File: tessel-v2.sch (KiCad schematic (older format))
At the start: 5 parts

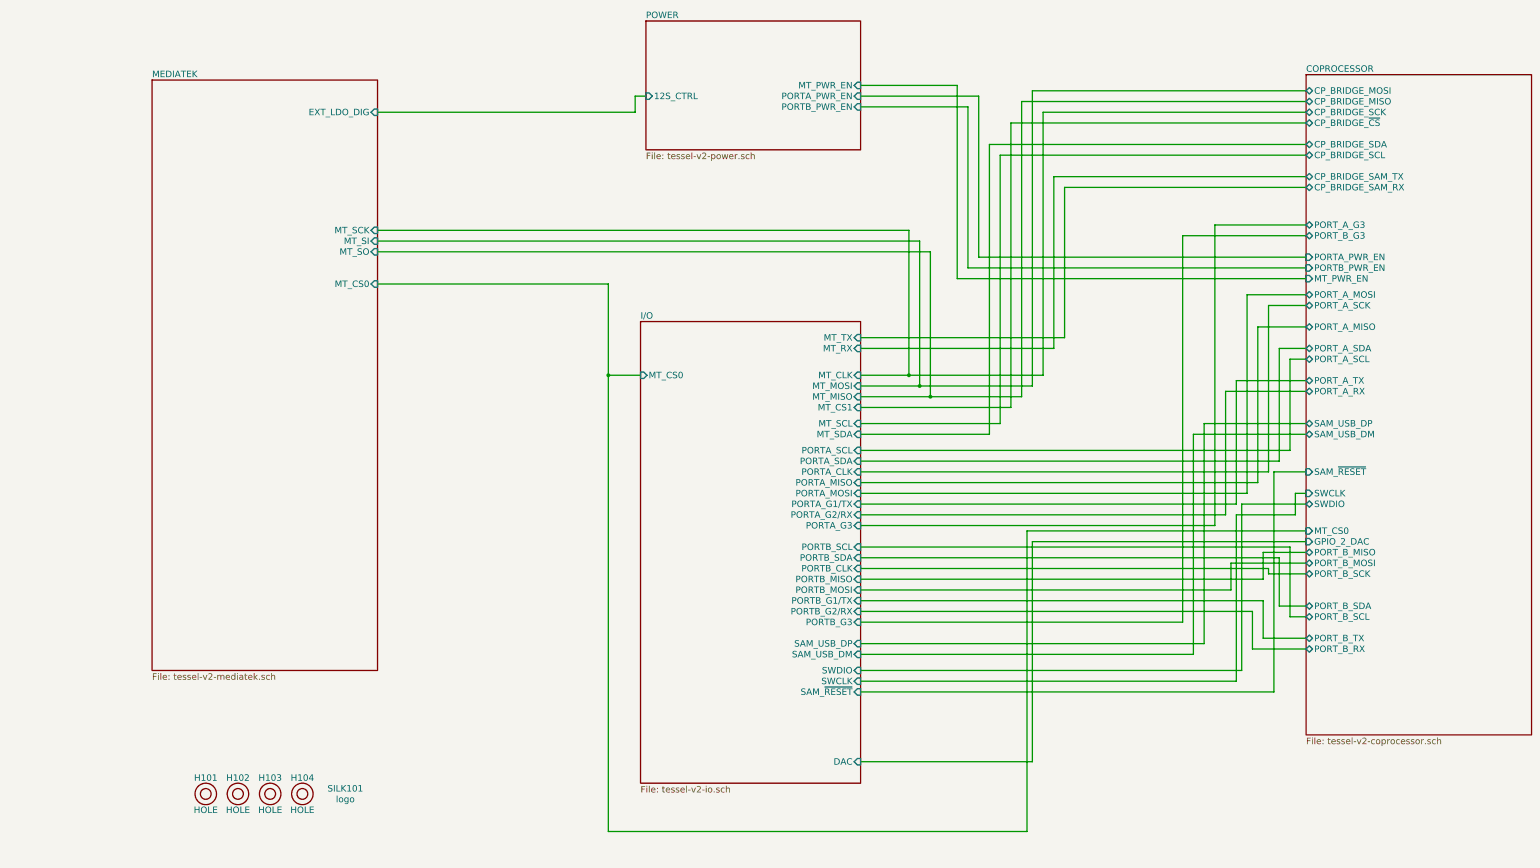
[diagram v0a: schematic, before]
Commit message: most schematic changes done, major refactoring underway
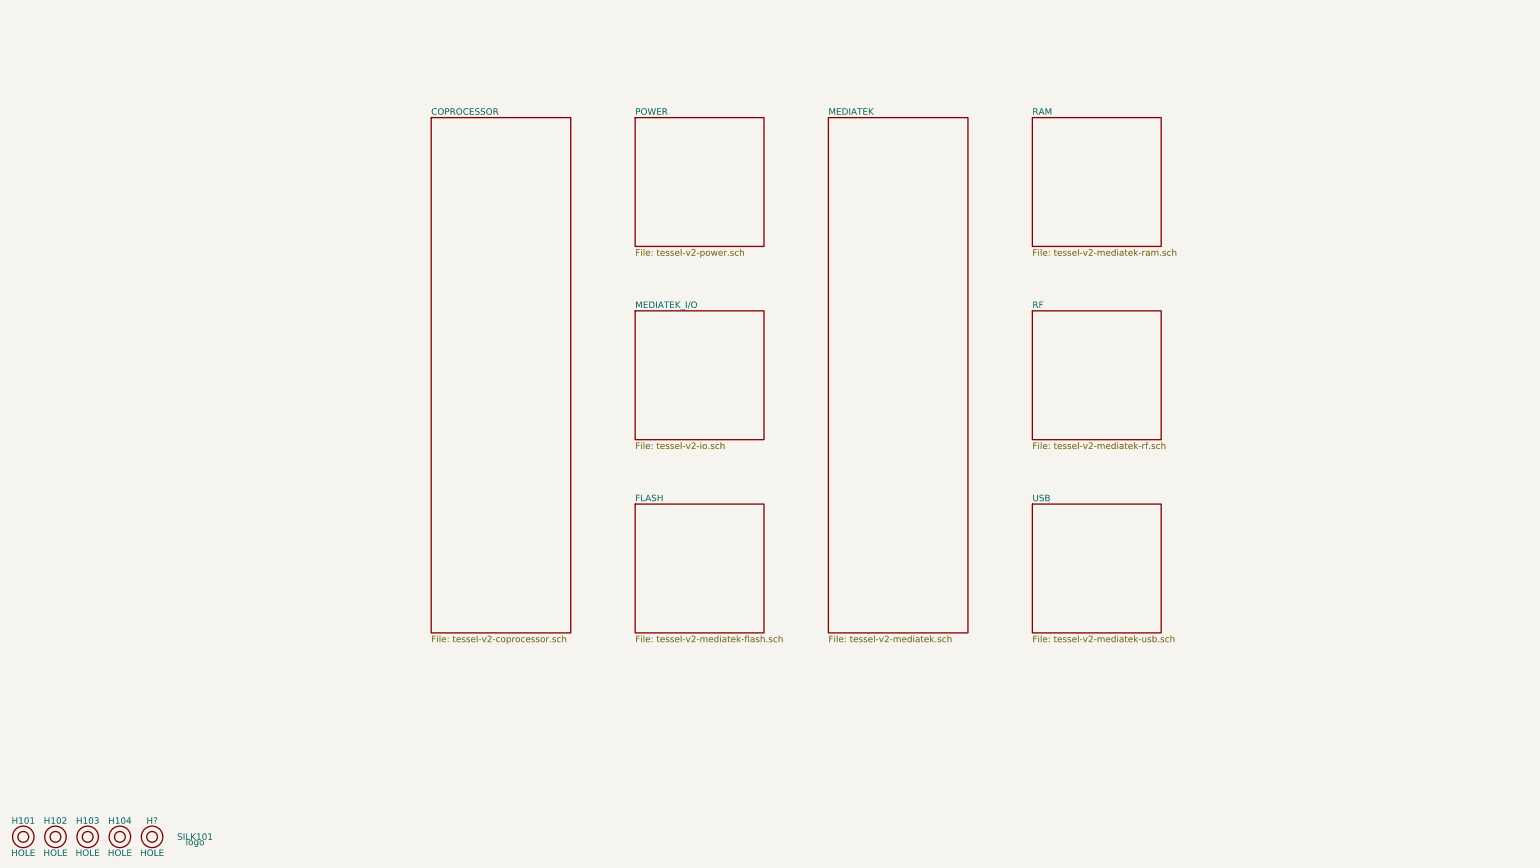
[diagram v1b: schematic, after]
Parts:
- added H?: HOLE, Mounting_Holes:MountingHole_2-5mm, symbol HOLE
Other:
- moved on the sheet: H101, H102, H103, H104

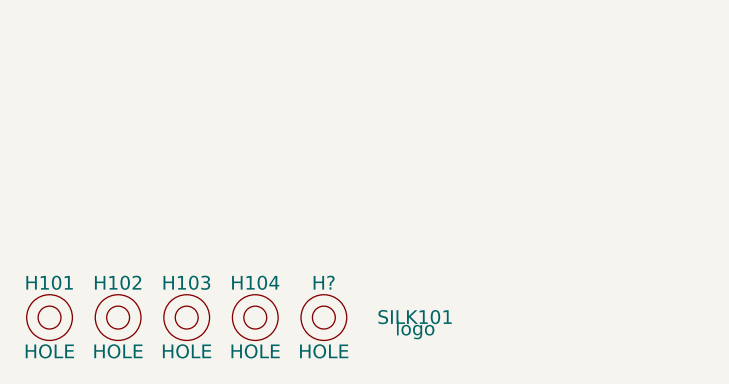
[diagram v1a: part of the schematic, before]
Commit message: reset annotation
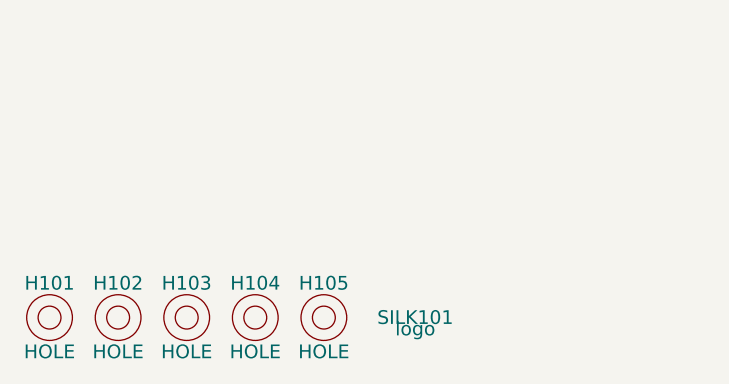
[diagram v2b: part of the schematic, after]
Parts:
- gave numbers to parts that had none: 1
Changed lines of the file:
@@
 $EndComp
 $Comp
-L HOLE H?
+L HOLE H105
 U 1 1 54EB1E4F
 P 2400 9800
-F 0 "H?" H 2400 9950 60  0000 C CNN
+F 0 "H105" H 2400 9950 60  0000 C CNN
 F 1 "HOLE" H 2400 9650 60  0000 C CNN
 F 2 "Mounting_Holes:MountingHole_2-5mm" H 2400 9800 60  0001 C CNN

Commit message: post-quick review from refactor
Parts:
- SILK101: footprint !Parts:TESSEL-HEXAGON-LOGO -> (none)
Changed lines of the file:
@@
 F 0 "SILK101" H 2800 9800 60  0000 C CNN
 F 1 "logo" H 2800 9750 60  0000 C CNN
-F 2 "!Parts:TESSEL-HEXAGON-LOGO" H 2800 9800 60  0001 C CNN
+F 2 "" H 2800 9800 60  0001 C CNN
 F 3 "" H 2800 9800 60  0000 C CNN
 	1    2800 9800

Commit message: value optimization for the sake of bom complexity
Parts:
- SILK101: footprint (none) -> !Parts:TESSEL-TEXT-LOGO-31.8mm8.1mm
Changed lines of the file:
@@
 F 0 "SILK101" H 2800 9800 60  0000 C CNN
 F 1 "logo" H 2800 9750 60  0000 C CNN
-F 2 "" H 2800 9800 60  0001 C CNN
+F 2 "!Parts:TESSEL-TEXT-LOGO-31.8mm8.1mm" H 2800 9800 60  0001 C CNN
 F 3 "" H 2800 9800 60  0000 C CNN
 	1    2800 9800

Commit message: back-propogated componet information, placed lots of things
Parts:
- SILK101: footprint !Parts:TESSEL-TEXT-LOGO-31.8mm8.1mm -> tm-kicad-lib:TESSEL-TEXT-LOGO-31.8mm8.1mm
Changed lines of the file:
@@
 F 0 "SILK101" H 2800 9800 60  0000 C CNN
 F 1 "logo" H 2800 9750 60  0000 C CNN
-F 2 "!Parts:TESSEL-TEXT-LOGO-31.8mm8.1mm" H 2800 9800 60  0001 C CNN
+F 2 "tm-kicad-lib:TESSEL-TEXT-LOGO-31.8mm8.1mm" H 2800 9800 60  0001 C CNN
 F 3 "" H 2800 9800 60  0000 C CNN
 	1    2800 9800

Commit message: placement completele! let the routing begin!
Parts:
- removed H105: HOLE, Mounting_Holes:MountingHole_2-5mm, symbol HOLE
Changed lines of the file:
@@
-	1    0    0    -1
-$EndComp
-$Comp
-L HOLE H105
-U 1 1 54EB1E4F
-P 2400 9800
-F 0 "H105" H 2400 9950 60  0000 C CNN
-F 1 "HOLE" H 2400 9650 60  0000 C CNN
-F 2 "Mounting_Holes:MountingHole_2-5mm" H 2400 9800 60  0001 C CNN
-F 3 "" H 2400 9800 60  0000 C CNN
-	1    2400 9800
 	1    0    0    -1
 $EndComp

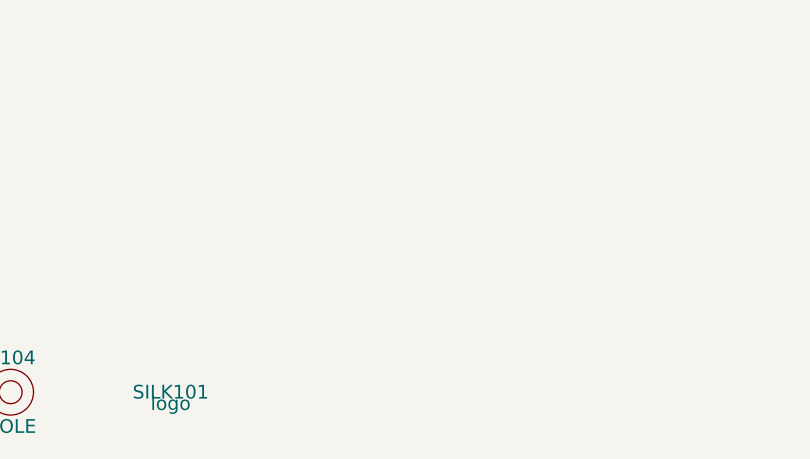
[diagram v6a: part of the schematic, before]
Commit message: added fiducials
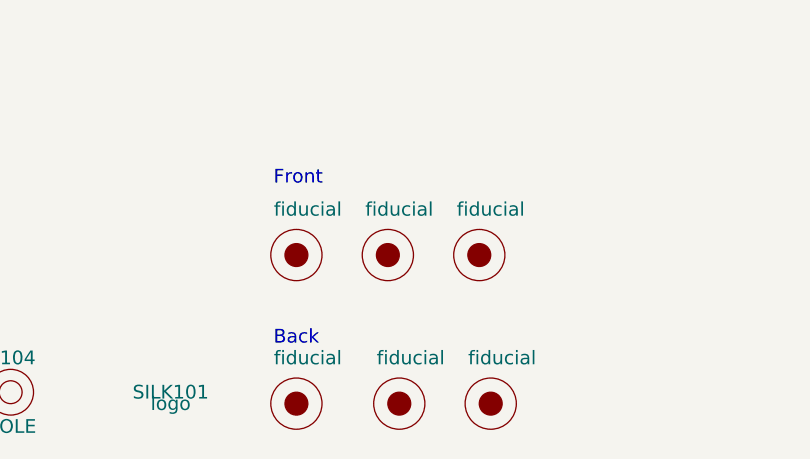
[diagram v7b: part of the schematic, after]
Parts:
- added F? (x6): fiducial, symbol fiducial
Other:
- note added: "Back"
- note added: "Front"
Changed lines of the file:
@@
 F1 "tessel-v2-mediatek-usb.sch" 60
 $EndSheet
+$Comp
+L fiducial F?
+U 1 1 54F4F9B2
+P 3350 9850
+F 0 "F?" H 3300 10150 60  0001 C CNN
+F 1 "fiducial" H 3400 10050 60  0000 C CNN
+F 2 "" H 3400 10050 60  0000 C CNN
+F 3 "" H 3400 10050 60  0000 C CNN
+	1    3350 9850
+	1    0    0    -1
+$EndComp
+$Comp
+L fiducial F?
+U 1 1 54F4F9D5
+P 3800 9850
+F 0 "F?" H 3750 10150 60  0001 C CNN
+F 1 "fiducial" H 3850 10050 60  0000 C CNN
+F 2 "" H 3850 10050 60  0000 C CNN
+F 3 "" H 3850 10050 60  0000 C CNN
+	1    3800 9850
+	1    0    0    -1
+$EndComp
+$Comp
+L fiducial F?
+U 1 1 54F4F9EE
+P 4200 9850
+F 0 "F?" H 4150 10150 60  0001 C CNN
+F 1 "fiducial" H 4250 10050 60  0000 C CNN
+F 2 "" H 4250 10050 60  0000 C CNN
+F 3 "" H 4250 10050 60  0000 C CNN
+	1    4200 9850
+	1    0    0    -1
+$EndComp
+$Comp
+L fiducial F?
+U 1 1 54F50161
+P 3350 9200
+F 0 "F?" H 3300 9500 60  0001 C CNN
+F 1 "fiducial" H 3400 9400 60  0000 C CNN
+F 2 "" H 3400 9400 60  0000 C CNN
+F 3 "" H 3400 9400 60  0000 C CNN
+	1    3350 9200
+	1    0    0    -1
+$EndComp
+$Comp
+L fiducial F?
+U 1 1 54F5017A
+P 3750 9200
+F 0 "F?" H 3700 9500 60  0001 C CNN
+F 1 "fiducial" H 3800 9400 60  0000 C CNN
+F 2 "" H 3800 9400 60  0000 C CNN
+F 3 "" H 3800 9400 60  0000 C CNN
+	1    3750 9200
+	1    0    0    -1
+$EndComp
+$Comp
+L fiducial F?
+U 1 1 54F50193
+P 4150 9200
+F 0 "F?" H 4100 9500 60  0001 C CNN
+F 1 "fiducial" H 4200 9400 60  0000 C CNN
+F 2 "" H 4200 9400 60  0000 C CNN
+F 3 "" H 4200 9400 60  0000 C CNN
+	1    4150 9200
+	1    0    0    -1
+$EndComp
+Text Notes 3250 8900 0    60   ~ 0
+Front
+Text Notes 3250 9600 0    60   ~ 0
+Back
 $EndSCHEMATC

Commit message: cleaned up schematics for release (tm-t2-03)
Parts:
- gave numbers to parts that had none: 6
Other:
- note added: "BACK"
- note added: "FRONT"
- note added: "HOLES, LOGOS, AND FIDUCIALS"
- note removed: "Back"
- note removed: "Front"
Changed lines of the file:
@@
 encoding utf-8
 Sheet 1 9
-Title "Tessel v2"
+Title "Tessel 2"
 Date ""
-Rev ""
+Rev "TM-T2-03"
 Comp "Technical Machine"
 Comment1 "Copyright 2015 Technical Machine Inc."
@@
 L logo SILK101
 U 1 1 54DD9FA3
-P 2800 9800
-F 0 "SILK101" H 2800 9800 60  0000 C CNN
-F 1 "logo" H 2800 9750 60  0000 C CNN
-F 2 "tm-kicad-lib:TESSEL-TEXT-LOGO-31.8mm8.1mm" H 2800 9800 60  0001 C CNN
-F 3 "" H 2800 9800 60  0000 C CNN
-	1    2800 9800
+P 2700 9800
+F 0 "SILK101" H 2700 9800 60  0000 C CNN
+F 1 "logo" H 2700 9750 60  0000 C CNN
+F 2 "tm-kicad-lib:TESSEL-TEXT-LOGO-31.8mm8.1mm" H 2700 9800 60  0001 C CNN
+F 3 "" H 2700 9800 60  0000 C CNN
+	1    2700 9800
 	1    0    0    -1
 $EndComp
@@
 $EndSheet
 $Comp
-L fiducial F?
+L fiducial F104
 U 1 1 54F4F9B2
-P 3350 9850
-F 0 "F?" H 3300 10150 60  0001 C CNN
-F 1 "fiducial" H 3400 10050 60  0000 C CNN
-F 2 "" H 3400 10050 60  0000 C CNN
-F 3 "" H 3400 10050 60  0000 C CNN
-	1    3350 9850
+P 4500 9800
+F 0 "F104" H 4500 9950 60  0000 C CNN
+F 1 "fiducial" H 4500 9750 60  0001 C CNN
+F 2 "" H 4550 10000 60  0000 C CNN
+F 3 "" H 4550 10000 60  0000 C CNN
+	1    4500 9800
 	1    0    0    -1
 $EndComp
 $Comp
-L fiducial F?
+L fiducial F105
 U 1 1 54F4F9D5
-P 3800 9850
-F 0 "F?" H 3750 10150 60  0001 C CNN
-F 1 "fiducial" H 3850 10050 60  0000 C CNN
-F 2 "" H 3850 10050 60  0000 C CNN
-F 3 "" H 3850 10050 60  0000 C CNN
-	1    3800 9850
+P 4800 9800
+F 0 "F105" H 4800 9950 60  0000 C CNN
+F 1 "fiducial" H 4800 9750 60  0001 C CNN
+F 2 "" H 4850 10000 60  0000 C CNN
+F 3 "" H 4850 10000 60  0000 C CNN
+	1    4800 9800
 	1    0    0    -1
 $EndComp
 $Comp
-L fiducial F?
+L fiducial F106
 U 1 1 54F4F9EE
-P 4200 9850
-F 0 "F?" H 4150 10150 60  0001 C CNN
-F 1 "fiducial" H 4250 10050 60  0000 C CNN
-F 2 "" H 4250 10050 60  0000 C CNN
-F 3 "" H 4250 10050 60  0000 C CNN
-	1    4200 9850
+P 5100 9800
+F 0 "F106" H 5100 9950 60  0000 C CNN
+F 1 "fiducial" H 5100 9750 60  0001 C CNN
+F 2 "" H 5150 10000 60  0000 C CNN
+F 3 "" H 5150 10000 60  0000 C CNN
+	1    5100 9800
 	1    0    0    -1
 $EndComp
 $Comp
-L fiducial F?
+L fiducial F101
 U 1 1 54F50161
-P 3350 9200
-F 0 "F?" H 3300 9500 60  0001 C CNN
-F 1 "fiducial" H 3400 9400 60  0000 C CNN
-F 2 "" H 3400 9400 60  0000 C CNN
-F 3 "" H 3400 9400 60  0000 C CNN
-	1    3350 9200
+P 3300 9800
+F 0 "F101" H 3300 9950 60  0000 C CNN
+F 1 "fiducial" H 3300 9750 60  0001 C CNN
+F 2 "" H 3350 10000 60  0000 C CNN
+F 3 "" H 3350 10000 60  0000 C CNN
+	1    3300 9800
 	1    0    0    -1
 $EndComp
 $Comp
-L fiducial F?
+L fiducial F102
 U 1 1 54F5017A
-P 3750 9200
-F 0 "F?" H 3700 9500 60  0001 C CNN
-F 1 "fiducial" H 3800 9400 60  0000 C CNN
-F 2 "" H 3800 9400 60  0000 C CNN
-F 3 "" H 3800 9400 60  0000 C CNN
-	1    3750 9200
+P 3600 9800
+F 0 "F102" H 3600 9950 60  0000 C CNN
+F 1 "fiducial" H 3600 9750 60  0001 C CNN
+F 2 "" H 3650 10000 60  0000 C CNN
+F 3 "" H 3650 10000 60  0000 C CNN
+	1    3600 9800
 	1    0    0    -1
 $EndComp
 $Comp
-L fiducial F?
+L fiducial F103
 U 1 1 54F50193
-P 4150 9200
-F 0 "F?" H 4100 9500 60  0001 C CNN
-F 1 "fiducial" H 4200 9400 60  0000 C CNN
-F 2 "" H 4200 9400 60  0000 C CNN
-F 3 "" H 4200 9400 60  0000 C CNN
-	1    4150 9200
+P 3900 9800
+F 0 "F103" H 3900 9950 60  0000 C CNN
+F 1 "fiducial" H 3900 9750 60  0001 C CNN
+F 2 "" H 3950 10000 60  0000 C CNN
+F 3 "" H 3950 10000 60  0000 C CNN
+	1    3900 9800
 	1    0    0    -1
 $EndComp
-Text Notes 3250 8900 0    60   ~ 0
-Front
-Text Notes 3250 9600 0    60   ~ 0
-Back
+Text Notes 3200 9500 0    60   ~ 0
+FRONT
+Text Notes 4400 9500 0    60   ~ 0
+BACK
+Text Notes 1200 9200 0    60   ~ 0
+HOLES, LOGOS, AND FIDUCIALS
 $EndSCHEMATC
